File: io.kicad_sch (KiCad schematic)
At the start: 67 parts, among them J10 JP_REL1_COM_12V, J12 JP_REL2_COM_12V, J13 JP_REL3_COM_12V, J14 Conn_REL1, J15 Conn_REL2, J16 Conn_REL3, J5 JP_REL4_COM_12V, J8 JP_REL5_COM_12V, J9 JP_REL6_COM_12V, K2 TIANBO-HJR-4102-L, K3 TIANBO-HJR-4102-L, K4 TIANBO-HJR-4102-L, K5 TIANBO-HJR-4102-L, K6 TIANBO-HJR-4102-L, K7 TIANBO-HJR-4102-L, Q2 BSS138, Q3 BSS138, Q4 BSS138, Q5 BSS138, Q6 BSS138, Q7 BSS138, U10 74HC595, U20 HC 151, X5 Conn_Rel2, X6 Conn_Rel1

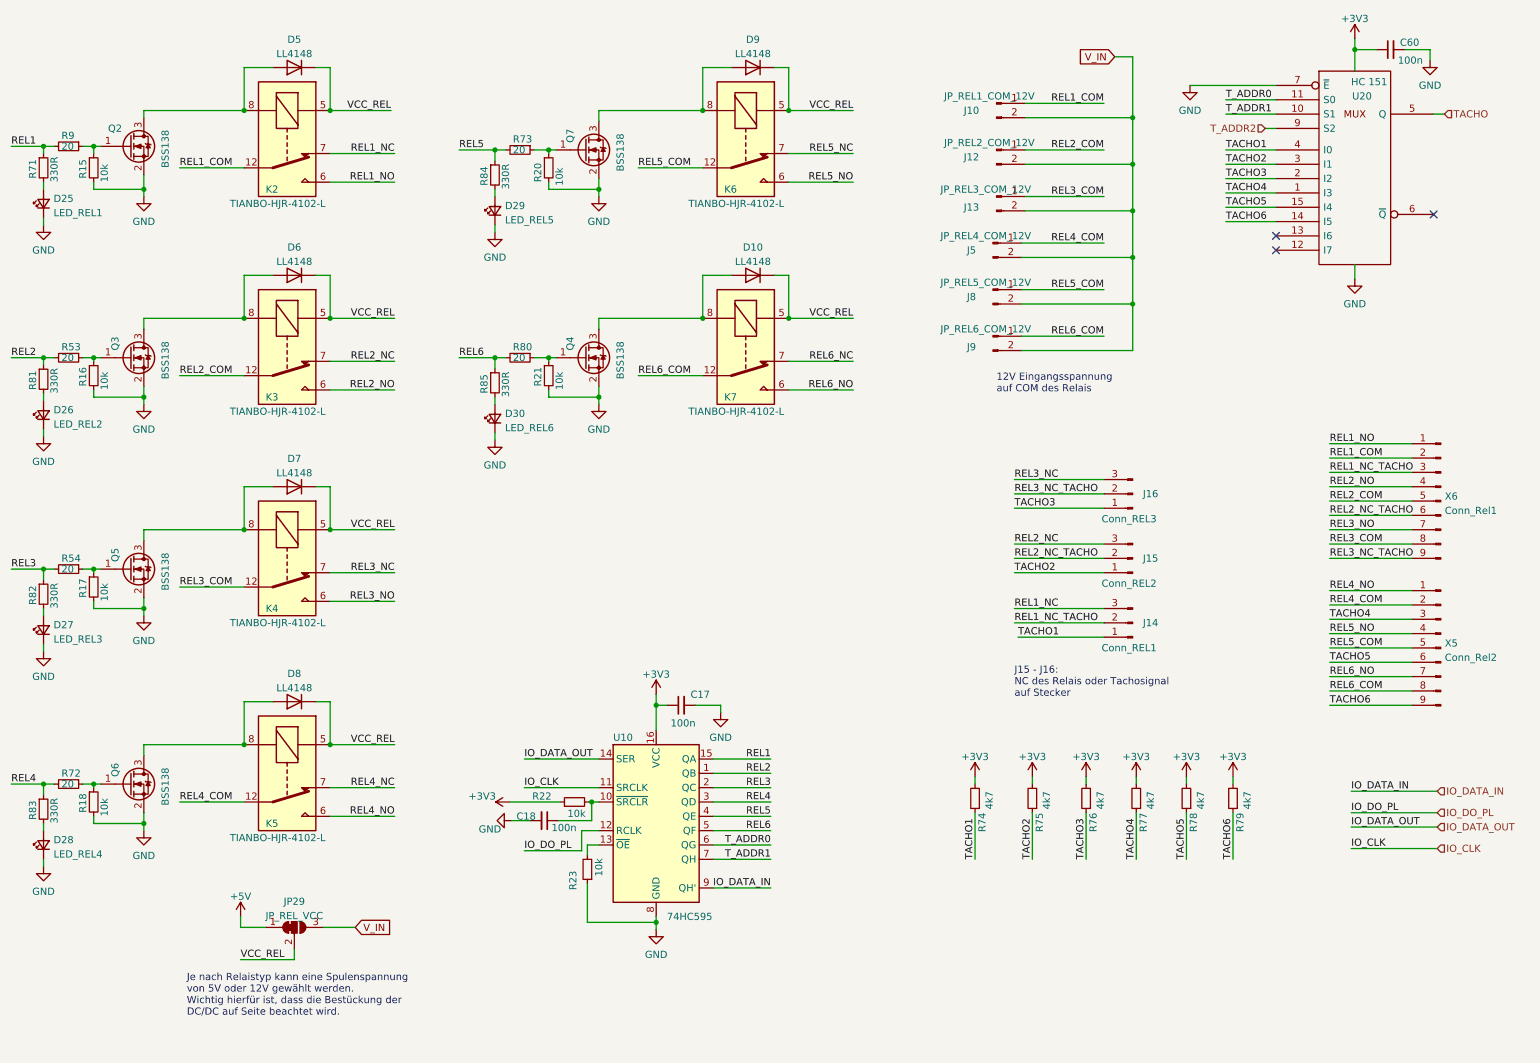
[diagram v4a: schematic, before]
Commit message: Improvements added (Ref 2.4.1)
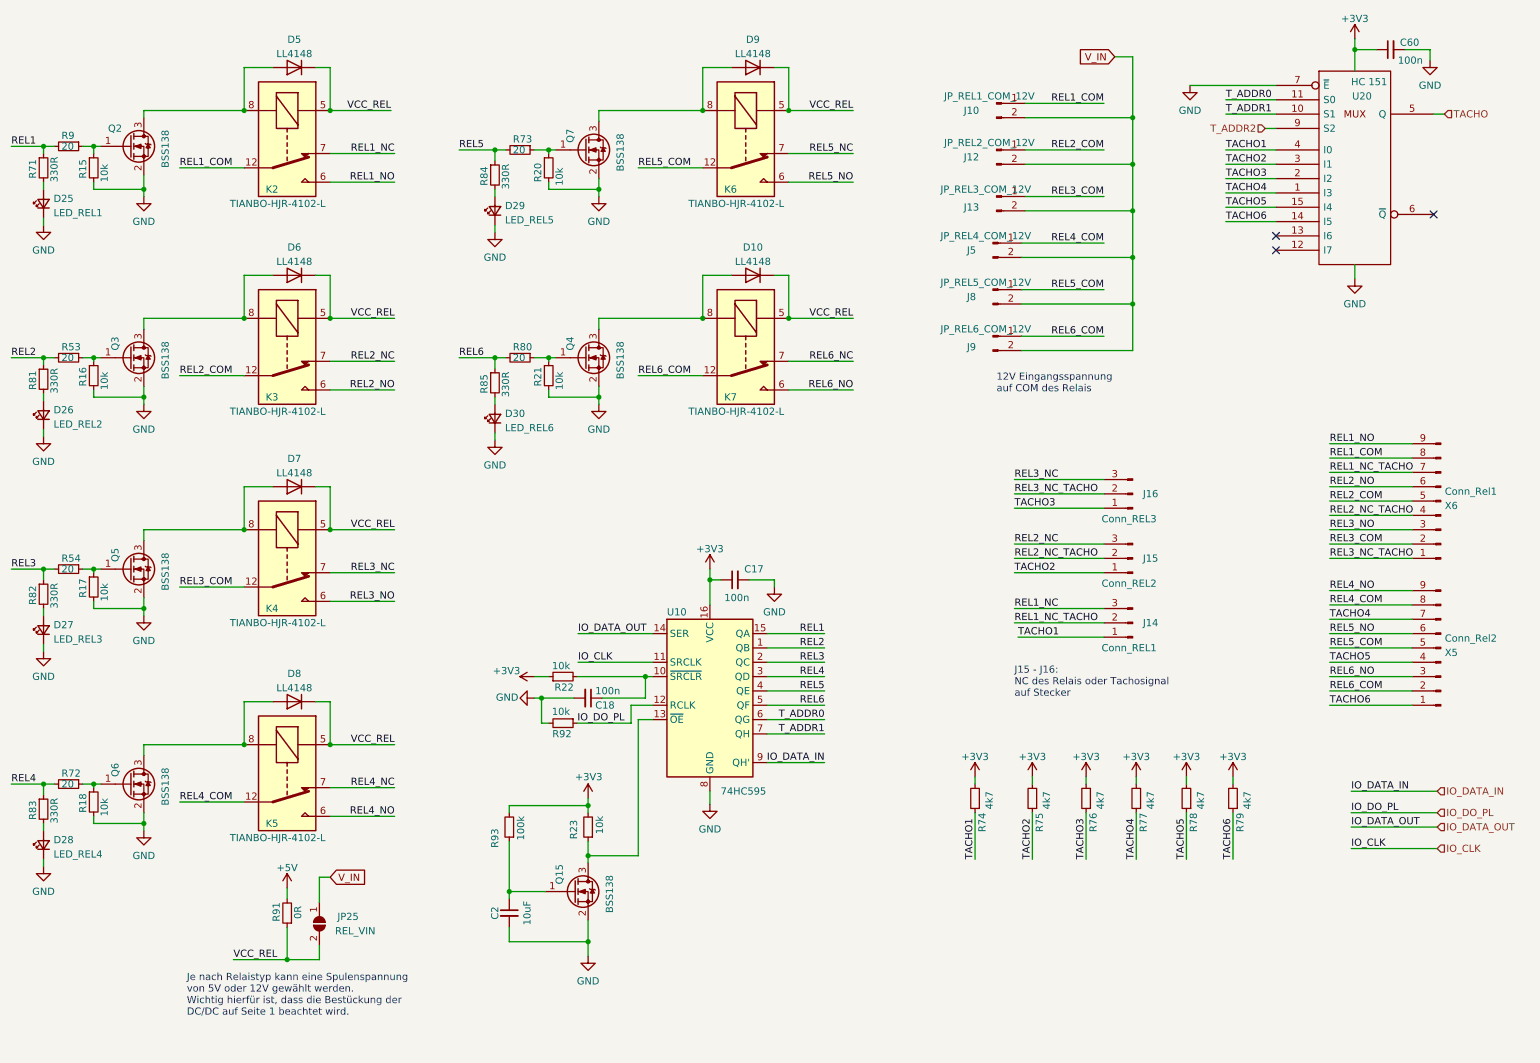
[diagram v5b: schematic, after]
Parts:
- removed JP29: JP_REL_VCC, Jumper:SolderJumper-3_P1.3mm_Bridged12_RoundedPad1.0x1.5mm_NumberLabels, symbol Jumper:SolderJumper_3_Bridged12
- added C2: 10uF, Capacitor_SMD:C_0603_1608Metric, symbol Device:C_Small
- added JP25: REL_VIN, Jumper:SolderJumper-2_P1.3mm_Open_RoundedPad1.0x1.5mm, symbol Jumper:SolderJumper_2_Open
- added Q15: BSS138, Package_TO_SOT_SMD:SOT-23, symbol Transistor_FET:BSS138
- added R91: 0R, Resistor_SMD:R_0603_1608Metric, symbol Device:R_Small
- added R92: 10k, Resistor_SMD:R_0603_1608Metric, symbol Device:R_Small
- added R93: 100k, Resistor_SMD:R_0603_1608Metric, symbol Device:R_Small
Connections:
- net +3V3: now also R23.2, R93.2
- net +5V: now also R91.2
- net GND: now also C2.2, Q15.2 (S), R92.2; no longer R23.1
- net IO_DO_PL: now also R92.1
- net REL1_COM: now also X6.8 (Pin_8); no longer X6.2 (Pin_2)
- net REL1_NC_TACHO: now also X6.7 (Pin_7); no longer X6.3 (Pin_3)
- net REL1_NO: now also X6.9 (Pin_9); no longer X6.1 (Pin_1)
- net REL2_NC_TACHO: now also X6.4 (Pin_4); no longer X6.6 (Pin_6)
- net REL2_NO: now also X6.6 (Pin_6); no longer X6.4 (Pin_4)
- net REL3_COM: now also X6.2 (Pin_2); no longer X6.8 (Pin_8)
- net REL3_NC_TACHO: now also X6.1 (Pin_1); no longer X6.9 (Pin_9)
- net REL3_NO: now also X6.3 (Pin_3); no longer X6.7 (Pin_7)
- net REL4_COM: now also X5.8 (Pin_8); no longer X5.2 (Pin_2)
- net REL4_NO: now also X5.9 (Pin_9); no longer X5.1 (Pin_1)
- net REL5_NO: now also X5.6 (Pin_6); no longer X5.4 (Pin_4)
- net REL6_COM: now also X5.2 (Pin_2); no longer X5.8 (Pin_8)
- net REL6_NO: now also X5.3 (Pin_3); no longer X5.7 (Pin_7)
- net TACHO4: now also X5.7 (Pin_7); no longer X5.3 (Pin_3)
- net TACHO5: now also X5.4 (Pin_4); no longer X5.6 (Pin_6)
- net TACHO6: now also X5.1 (Pin_1); no longer X5.9 (Pin_9)
- net VCC_REL: now also JP25.2 (B), R91.1
- net V_IN: now also JP25.1 (A)
- net at U10.13 (~{OE}): now also R23.1, Q15.3 (D); no longer R23.2
- new net: C2.1, Q15.1 (G), R93.1
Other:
- note added: "Je nach Relaistyp kann eine Spulenspannung von 5V oder 12V gewählt werden. Wichtig hierfür ist, dass die Bestückung der DC/DC auf Seite 1 beachtet wird."
- note removed: "Je nach Relaistyp kann eine Spulenspannung von 5V oder 12V gewählt werden. Wichtig hierfür ist, dass die Bestückung der DC/DC auf Seite beachtet wird."
- moved on the sheet: C17, C18, R22, R23, U10, X5, X6
